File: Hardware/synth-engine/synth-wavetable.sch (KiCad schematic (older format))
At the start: 0 parts

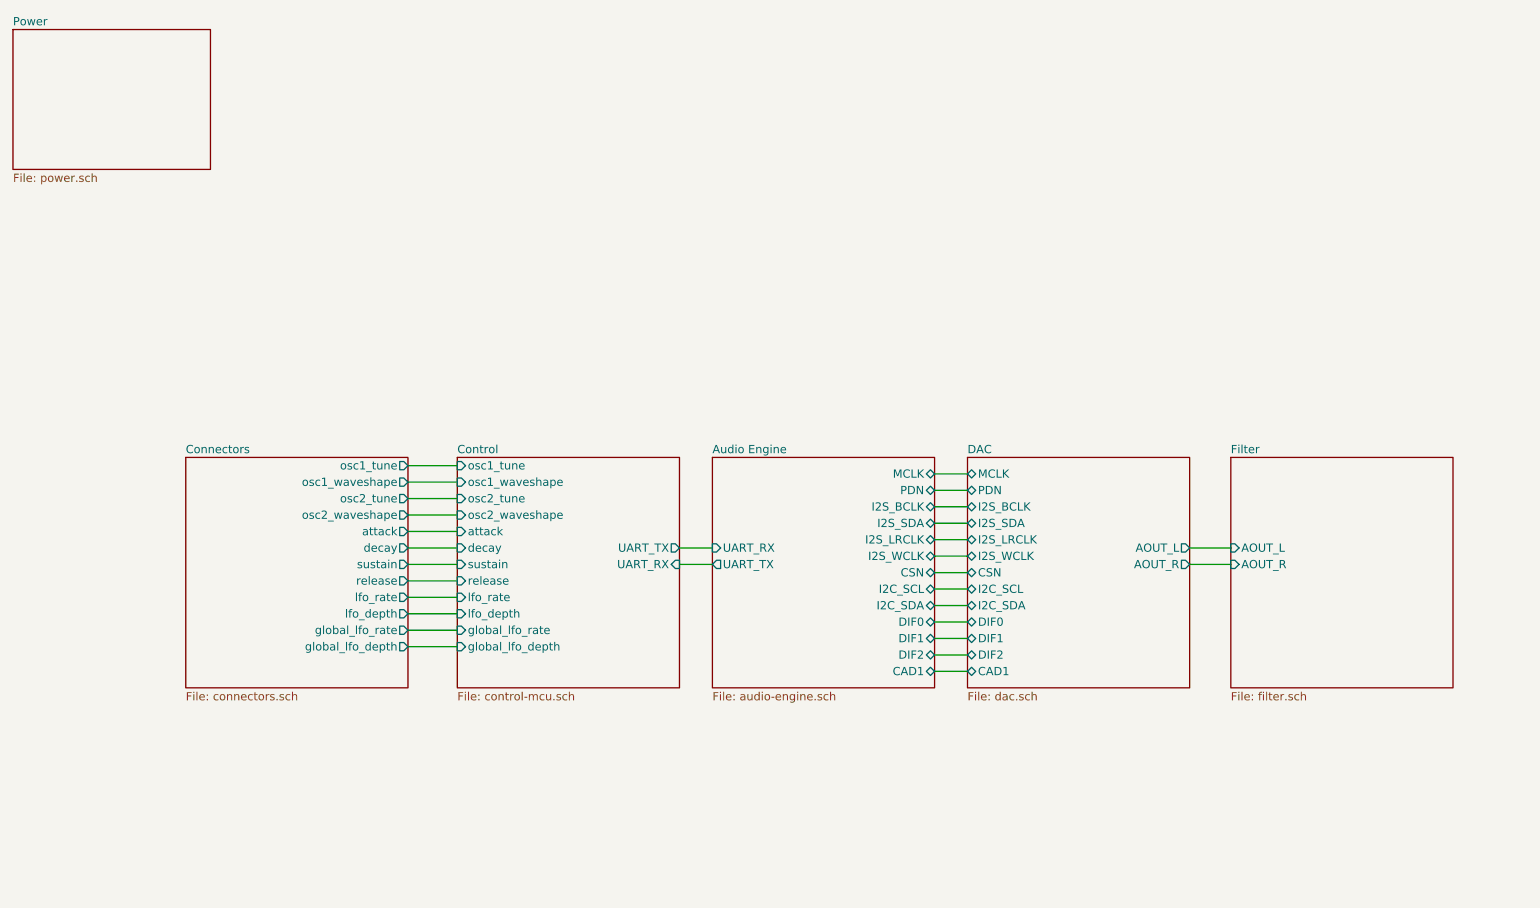
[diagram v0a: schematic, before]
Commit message: initial routing complete. Still need to do ground plane pours. There are still some issues with incorrect footprints.
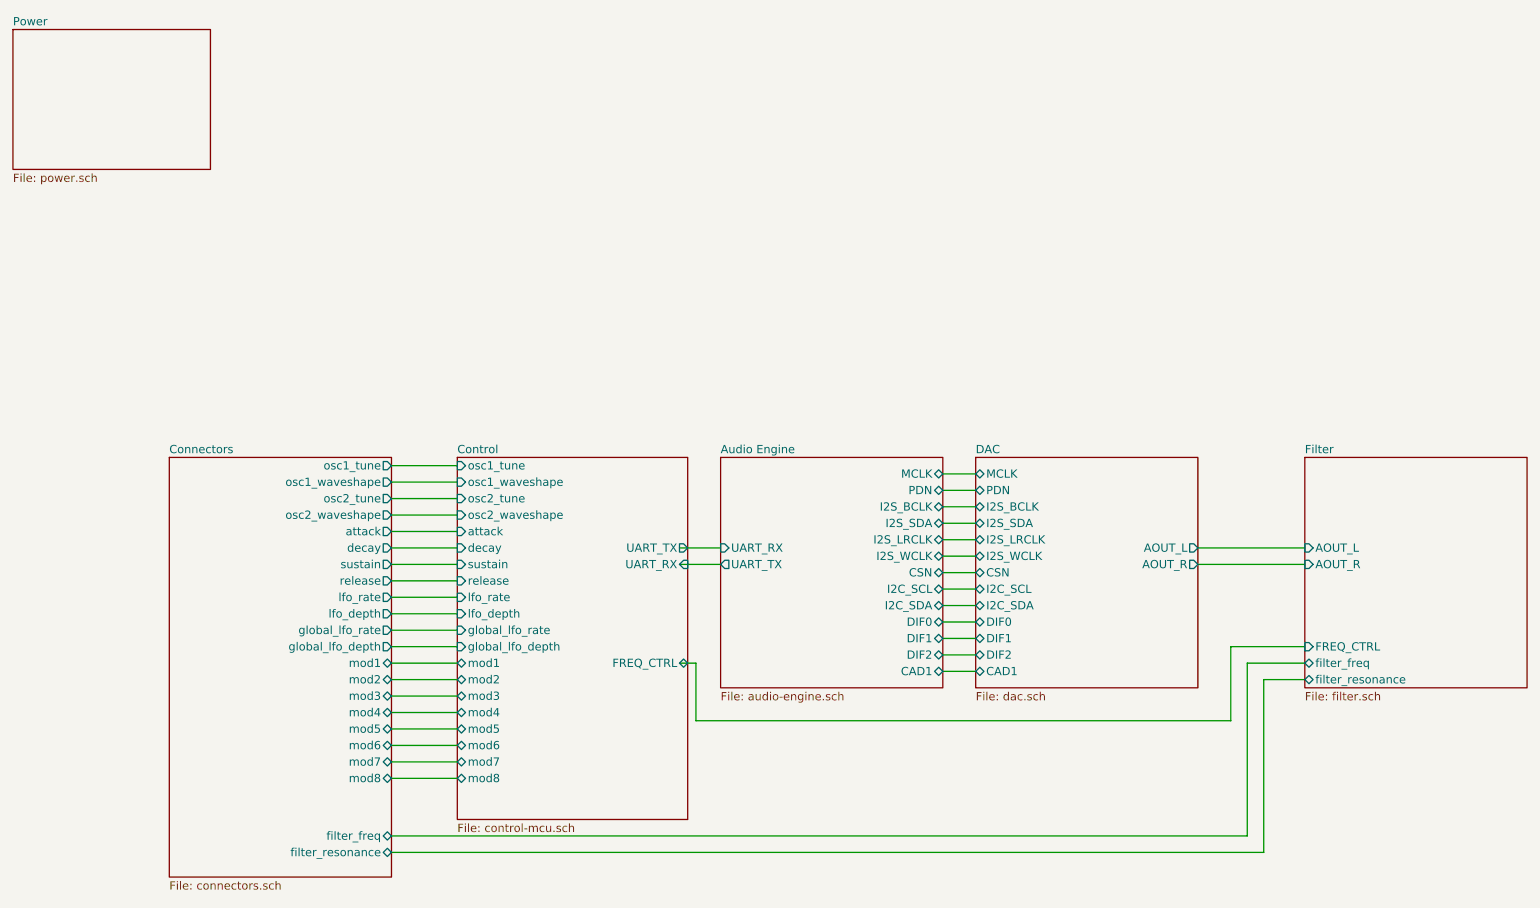
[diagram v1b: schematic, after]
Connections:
- wire segments 29 -> 48
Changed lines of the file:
@@
 $EndDescr
 $Sheet
-S 3600 3500 1350 1400
+S 3600 3500 1400 2200
 U 5DDBDEEA
 F0 "Control" 50
 F1 "control-mcu.sch" 50
-F2 "UART_TX" O R 4950 4050 50
-F3 "UART_RX" I R 4950 4150 50
+F2 "UART_TX" O R 5000 4050 50
+F3 "UART_RX" I R 5000 4150 50
 F4 "osc1_tune" I L 3600 3550 50
 F5 "osc1_waveshape" I L 3600 3650 50
@@
 F14 "global_lfo_rate" I L 3600 4550 50
 F15 "global_lfo_depth" I L 3600 4650 50
-$EndSheet
-$Sheet
-S 5150 3500 1350 1400
+F16 "FREQ_CTRL" B R 5000 4750 50
+F17 "mod1" B L 3600 4750 50
+F18 "mod2" B L 3600 4850 50
+F19 "mod3" B L 3600 4950 50
+F20 "mod4" B L 3600 5050 50
+F21 "mod5" B L 3600 5150 50
+F22 "mod6" B L 3600 5250 50
+F23 "mod7" B L 3600 5350 50
+F24 "mod8" B L 3600 5450 50
+$EndSheet
+$Sheet
+S 5200 3500 1350 1400
 U 5DDC7BB6
 F0 "Audio Engine" 50
 F1 "audio-engine.sch" 50
-F2 "PDN" B R 6500 3700 50
-F3 "I2S_BCLK" B R 6500 3800 50
-F4 "I2S_SDA" B R 6500 3900 50
-F5 "I2S_LRCLK" B R 6500 4000 50
-F6 "I2S_WCLK" B R 6500 4100 50
-F7 "CSN" B R 6500 4200 50
-F8 "I2C_SCL" B R 6500 4300 50
-F9 "I2C_SDA" B R 6500 4400 50
-F10 "DIF0" B R 6500 4500 50
-F11 "DIF1" B R 6500 4600 50
-F12 "DIF2" B R 6500 4700 50
-F13 "MCLK" B R 6500 3600 50
-F14 "CAD1" B R 6500 4800 50
-F15 "UART_TX" O L 5150 4150 50
-F16 "UART_RX" I L 5150 4050 50
-$EndSheet
-$Sheet
-S 8300 3500 1350 1400
+F2 "PDN" B R 6550 3700 50
+F3 "I2S_BCLK" B R 6550 3800 50
+F4 "I2S_SDA" B R 6550 3900 50
+F5 "I2S_LRCLK" B R 6550 4000 50
+F6 "I2S_WCLK" B R 6550 4100 50
+F7 "CSN" B R 6550 4200 50
+F8 "I2C_SCL" B R 6550 4300 50
+F9 "I2C_SDA" B R 6550 4400 50
+F10 "DIF0" B R 6550 4500 50
+F11 "DIF1" B R 6550 4600 50
+F12 "DIF2" B R 6550 4700 50
+F13 "MCLK" B R 6550 3600 50
+F14 "CAD1" B R 6550 4800 50
+F15 "UART_TX" O L 5200 4150 50
+F16 "UART_RX" I L 5200 4050 50
+$EndSheet
+$Sheet
+S 8750 3500 1350 1400
 U 5DDC7E61
 F0 "Filter" 50
 F1 "filter.sch" 50
-F2 "AOUT_L" I L 8300 4050 50
-F3 "AOUT_R" I L 8300 4150 50
+F2 "AOUT_L" I L 8750 4050 50
+F3 "AOUT_R" I L 8750 4150 50
+F4 "FREQ_CTRL" I L 8750 4650 50
+F5 "filter_freq" B L 8750 4750 50
+F6 "filter_resonance" B L 8750 4850 50
 $EndSheet
 $Sheet
@@
 $EndSheet
 $Sheet
-S 6700 3500 1350 1400
+S 6750 3500 1350 1400
 U 5DD9C8DD
 F0 "DAC" 50
 F1 "dac.sch" 50
-F2 "MCLK" B L 6700 3600 50
-F3 "PDN" B L 6700 3700 50
-F4 "I2S_BCLK" B L 6700 3800 50
-F5 "I2S_SDA" B L 6700 3900 50
-F6 "I2S_LRCLK" B L 6700 4000 50
-F7 "I2S_WCLK" B L 6700 4100 50
-F8 "CSN" B L 6700 4200 50
-F9 "I2C_SCL" B L 6700 4300 50
-F10 "I2C_SDA" B L 6700 4400 50
-F11 "DIF0" B L 6700 4500 50
-F12 "DIF1" B L 6700 4600 50
-F13 "DIF2" B L 6700 4700 50
-F14 "CAD1" B L 6700 4800 50
-F15 "AOUT_L" O R 8050 4050 50
-F16 "AOUT_R" O R 8050 4150 50
-$EndSheet
-Wire Wire Line
-	6500 3600 6700 3600
-Wire Wire Line
-	6700 3700 6500 3700
-Wire Wire Line
-	6500 3800 6700 3800
-Wire Wire Line
-	6700 3900 6500 3900
-Wire Wire Line
-	6500 4000 6700 4000
-Wire Wire Line
-	6700 4100 6500 4100
-Wire Wire Line
-	6500 4200 6700 4200
-Wire Wire Line
-	6700 4300 6500 4300
-Wire Wire Line
-	6500 4400 6700 4400
-Wire Wire Line
-	6700 4500 6500 4500
-Wire Wire Line
-	6500 4600 6700 4600
-Wire Wire Line
-	6700 4700 6500 4700
-Wire Wire Line
-	6500 4800 6700 4800
-Wire Wire Line
-	8050 4050 8300 4050
-Wire Wire Line
-	8050 4150 8300 4150
-Wire Wire Line
-	4950 4150 5150 4150
-Wire Wire Line
-	5150 4050 4950 4050
-$Sheet
-S 1950 3500 1350 1400
+F2 "MCLK" B L 6750 3600 50
+F3 "PDN" B L 6750 3700 50
+F4 "I2S_BCLK" B L 6750 3800 50
+F5 "I2S_SDA" B L 6750 3900 50
+F6 "I2S_LRCLK" B L 6750 4000 50
+F7 "I2S_WCLK" B L 6750 4100 50
+F8 "CSN" B L 6750 4200 50
+F9 "I2C_SCL" B L 6750 4300 50
+F10 "I2C_SDA" B L 6750 4400 50
+F11 "DIF0" B L 6750 4500 50
+F12 "DIF1" B L 6750 4600 50
+F13 "DIF2" B L 6750 4700 50
+F14 "CAD1" B L 6750 4800 50
+F15 "AOUT_L" O R 8100 4050 50
+F16 "AOUT_R" O R 8100 4150 50
+$EndSheet
+Wire Wire Line
+	6550 3600 6750 3600
+Wire Wire Line
+	6750 3700 6550 3700
+Wire Wire Line
+	6550 3800 6750 3800
+Wire Wire Line
+	6750 3900 6550 3900
+Wire Wire Line
+	6550 4000 6750 4000
+Wire Wire Line
+	6750 4100 6550 4100
+Wire Wire Line
+	6550 4200 6750 4200
+Wire Wire Line
+	6750 4300 6550 4300
+Wire Wire Line
+	6550 4400 6750 4400
+Wire Wire Line
+	6750 4500 6550 4500
+Wire Wire Line
+	6550 4600 6750 4600
+Wire Wire Line
+	6750 4700 6550 4700
+Wire Wire Line
+	6550 4800 6750 4800
+Wire Wire Line
+	8100 4050 8750 4050
+Wire Wire Line
+	8100 4150 8750 4150
+Wire Wire Line
+	4950 4150 5200 4150
+Wire Wire Line
+	5200 4050 4950 4050
+$Sheet
+S 1850 3500 1350 2550
 U 5DDCA8E8
 F0 "Connectors" 50
 F1 "connectors.sch" 50
-F2 "osc1_tune" O R 3300 3550 50
-F3 "osc1_waveshape" O R 3300 3650 50
-F4 "osc2_tune" O R 3300 3750 50
-F5 "osc2_waveshape" O R 3300 3850 50
-F6 "attack" O R 3300 3950 50
-F7 "decay" O R 3300 4050 50
-F8 "sustain" O R 3300 4150 50
-F9 "release" O R 3300 4250 50
-F10 "lfo_rate" O R 3300 4350 50
-F11 "lfo_depth" O R 3300 4450 50
-F12 "global_lfo_rate" O R 3300 4550 50
-F13 "global_lfo_depth" O R 3300 4650 50
-$EndSheet
-Wire Wire Line
-	3300 3550 3600 3550
-Wire Wire Line
-	3300 3650 3600 3650
-Wire Wire Line
-	3300 3750 3600 3750
-Wire Wire Line
-	3300 3850 3600 3850
-Wire Wire Line
-	3300 3950 3600 3950
-Wire Wire Line
-	3300 4050 3600 4050
-Wire Wire Line
-	3300 4150 3600 4150
-Wire Wire Line
-	3300 4250 3600 4250
-Wire Wire Line
-	3300 4350 3600 4350
-Wire Wire Line
-	3300 4450 3600 4450
-Wire Wire Line
-	3300 4550 3600 4550
-Wire Wire Line
-	3300 4650 3600 4650
+F2 "osc1_tune" O R 3200 3550 50
+F3 "osc1_waveshape" O R 3200 3650 50
+F4 "osc2_tune" O R 3200 3750 50
+F5 "osc2_waveshape" O R 3200 3850 50
+F6 "attack" O R 3200 3950 50
+F7 "decay" O R 3200 4050 50
+F8 "sustain" O R 3200 4150 50
+F9 "release" O R 3200 4250 50
+F10 "lfo_rate" O R 3200 4350 50
+F11 "lfo_depth" O R 3200 4450 50
+F12 "global_lfo_rate" O R 3200 4550 50
+F13 "global_lfo_depth" O R 3200 4650 50
+F14 "filter_freq" B R 3200 5800 50
+F15 "filter_resonance" B R 3200 5900 50
+F16 "mod1" B R 3200 4750 50
+F17 "mod2" B R 3200 4850 50
+F18 "mod3" B R 3200 4950 50
+F19 "mod4" B R 3200 5050 50
+F20 "mod5" B R 3200 5150 50
+F21 "mod6" B R 3200 5250 50
+F22 "mod7" B R 3200 5350 50
+F23 "mod8" B R 3200 5450 50
+$EndSheet
+Wire Wire Line
+	3200 3550 3600 3550
+Wire Wire Line
+	3200 3650 3600 3650
+Wire Wire Line
+	3200 3750 3600 3750
+Wire Wire Line
+	3200 3850 3600 3850
+Wire Wire Line
+	3200 3950 3600 3950
+Wire Wire Line
+	3200 4050 3600 4050
+Wire Wire Line
+	3200 4150 3600 4150
+Wire Wire Line
+	3200 4250 3600 4250
+Wire Wire Line
+	3200 4350 3600 4350
+Wire Wire Line
+	3200 4450 3600 4450
+Wire Wire Line
+	3200 4550 3600 4550
+Wire Wire Line
+	3200 4650 3600 4650
+Wire Wire Line
+	8400 5800 8400 4750
+Wire Wire Line
+	8400 4750 8750 4750
+Wire Wire Line
+	8500 5900 8500 4850
+Wire Wire Line
+	8500 4850 8750 4850
+Wire Wire Line
+	4950 4750 5050 4750
+Wire Wire Line
+	5050 4750 5050 5100
+Wire Wire Line
+	5050 5100 8300 5100
+Wire Wire Line
+	8300 5100 8300 4650
+Wire Wire Line
+	8300 4650 8750 4650
+Wire Wire Line
+	3200 5900 8500 5900
+Wire Wire Line
+	3200 5800 8400 5800
+Wire Wire Line
+	3200 4750 3600 4750
+Wire Wire Line
+	3600 4850 3200 4850
+Wire Wire Line
+	3200 4950 3600 4950
+Wire Wire Line
+	3600 5050 3200 5050
+Wire Wire Line
+	3200 5150 3600 5150
+Wire Wire Line
+	3600 5250 3200 5250
+Wire Wire Line
+	3200 5350 3600 5350
+Wire Wire Line
+	3600 5450 3200 5450
 $EndSCHEMATC
